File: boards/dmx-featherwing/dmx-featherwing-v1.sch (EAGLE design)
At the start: 4 parts, among them U2 MAX3468CSA

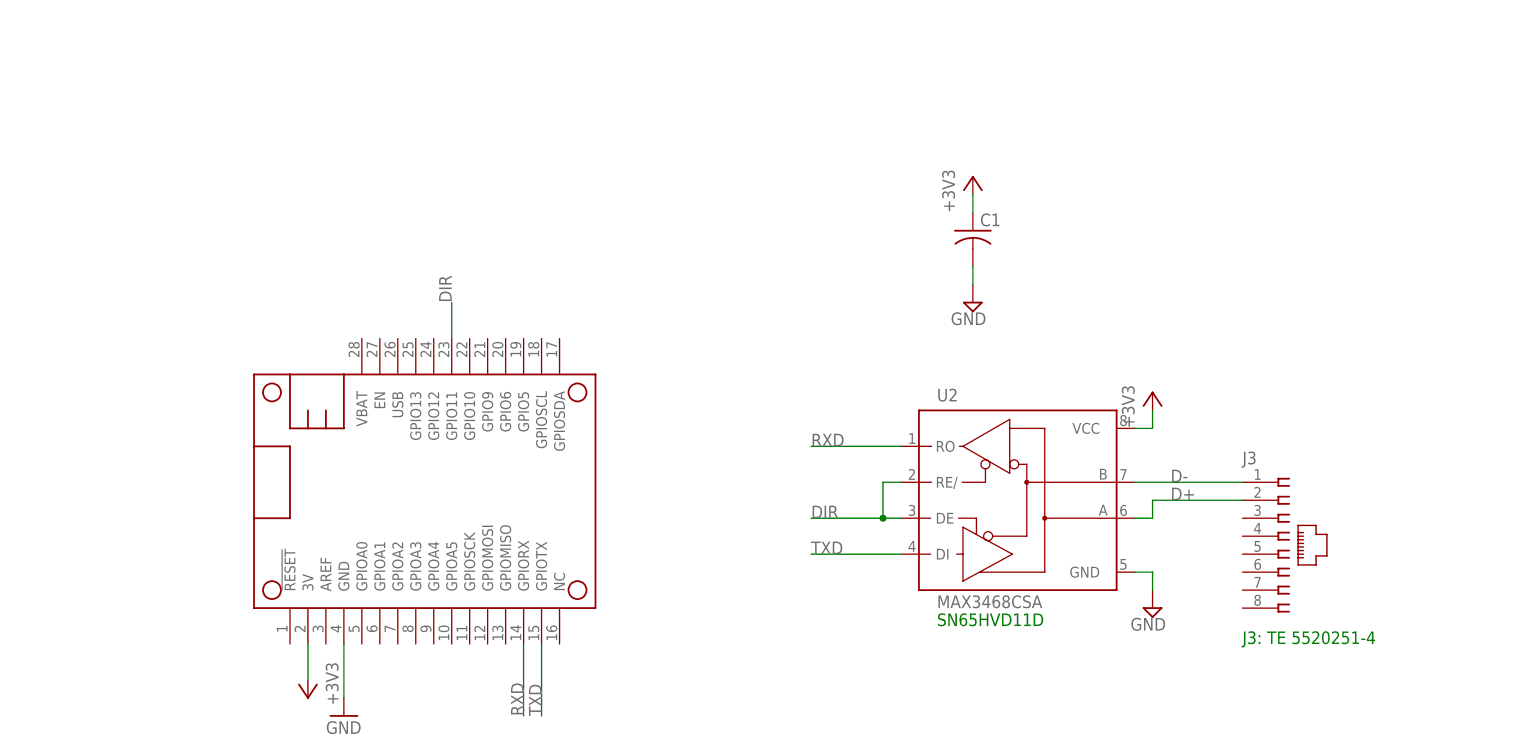
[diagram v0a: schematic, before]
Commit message: Added termination resistor, ESD protection, and chassis ground.
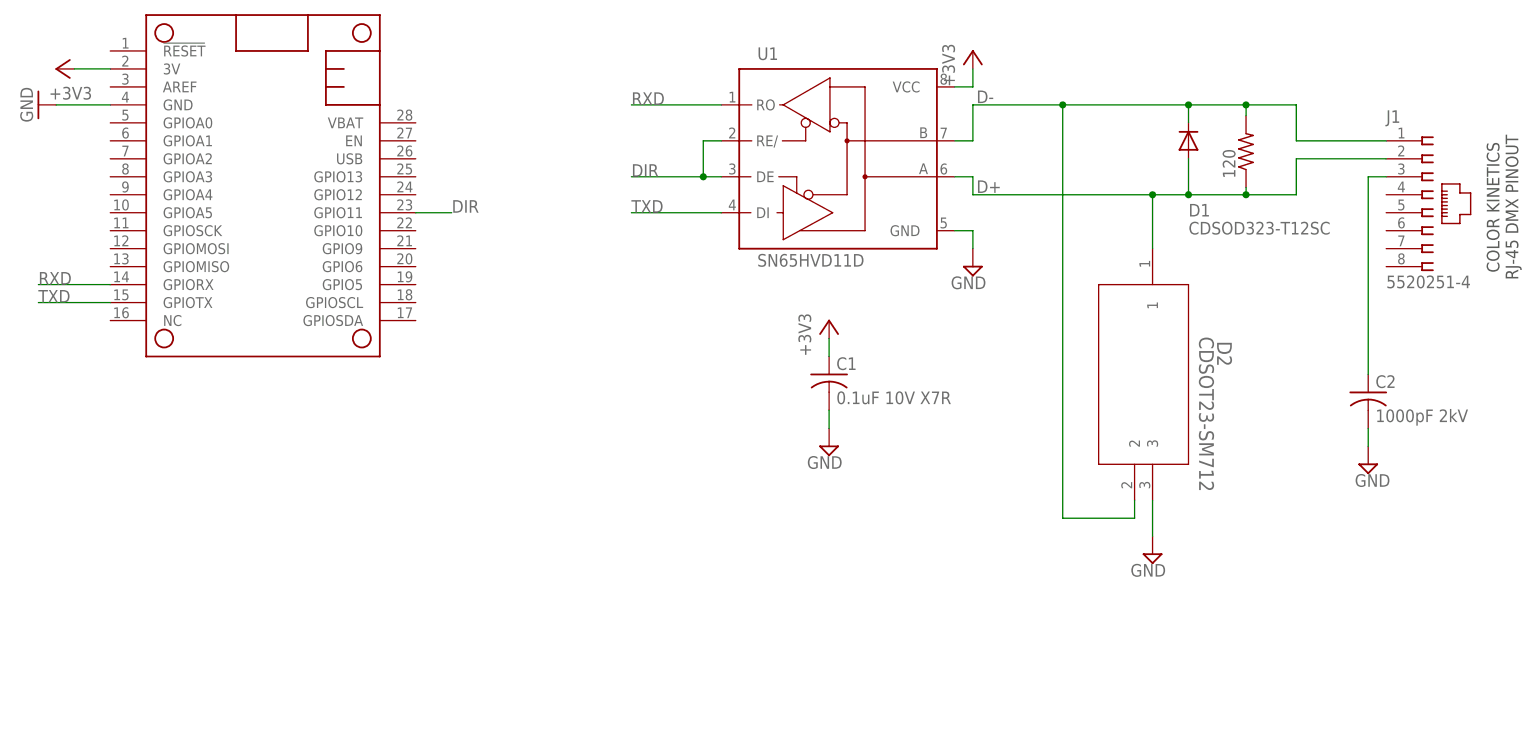
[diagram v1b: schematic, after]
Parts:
- removed J3: (no value), con-amp:520251-4
- removed U2: MAX3468CSA, maxim:MAX3468CSA
- added 120: (no value), rcl:R-US_R0805
- added C2: 1000pF 2kV, rcl:C-USC1206K
- added D1: CDSOD323-T12SC, diode:DIODE-SOD323-W
- added D2: CDSOT23-SM712, CDSOT23-SM712:CDSOT23-SM712
- added J1: 5520251-4, TE 5520251-4:5520251-4
- added U1: SN65HVD11D, maxim:MAX3468CSA
- C1: value (none) -> 0.1uF 10V X7R
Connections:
- new net N$1: C2.1, J1.3
- net +3V3: now also U1.VCC; no longer U2.VCC
- net D+: now also 120.1, D1.A, D2.1, J1.2, U1.A; no longer J3.2, U2.A
- net D-: now also 120.2, D1.C, D2.2, J1.1, U1.B; no longer J3.1, U2.B
- net DIR: now also U1.DE, U1.RE/; no longer U2.DE, U2.RE/
- net GND: now also C2.2, D2.3, U1.GND; no longer U2.GND
- net RXD: now also U1.RO; no longer U2.RO
- net TXD: now also U1.DI; no longer U2.DI
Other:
- note added: "COLOR KINETICS RJ-45 DMX PINOUT"
- note removed: "J3: TE 5520251-4"
- note removed: "SN65HVD11D"
- moved on the sheet: C1

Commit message: fixed R1 name/value, moved DIR label to correct pin
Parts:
- R1: value (none) -> 120
- renumbered 120 to R1
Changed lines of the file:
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@@
 <part name="C2" library="rcl" deviceset="C-US" device="C1206K" value="1000pF 2kV"/>
 <part name="SUPPLY1" library="supply2" deviceset="GND" device=""/>
-<part name="120" library="rcl" deviceset="R-US_" device="R0805"/>
+<part name="R1" library="rcl" deviceset="R-US_" device="R0805" value="120"/>
 </parts>
 <sheets>
@@
 <attribute name="VALUE" x="203.835" y="100.965" size="1.778" layer="96"/>
 </instance>
-<instance part="120" gate="G$1" x="188.468" y="148.336" rot="R90"/>
+<instance part="R1" gate="G$1" x="188.468" y="148.336" rot="R90"/>
 </instances>
 <busses>
@@
 <wire x1="162.56" y1="96.52" x2="162.56" y2="154.94" width="0.1524" layer="91"/>
 <junction x="162.56" y="154.94"/>
-<pinref part="120" gate="G$1" pin="2"/>
+<pinref part="R1" gate="G$1" pin="2"/>
 <wire x1="188.468" y1="153.416" x2="188.468" y2="154.94" width="0.1524" layer="91"/>
 <junction x="188.468" y="154.94"/>
@@
 <wire x1="175.26" y1="134.62" x2="175.26" y2="142.24" width="0.1524" layer="91"/>
 <junction x="175.26" y="142.24"/>
-<pinref part="120" gate="G$1" pin="1"/>
+<pinref part="R1" gate="G$1" pin="1"/>
 <wire x1="188.468" y1="143.256" x2="188.468" y2="142.24" width="0.1524" layer="91"/>
 <junction x="188.468" y="142.24"/>
